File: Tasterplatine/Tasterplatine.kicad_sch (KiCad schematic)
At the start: 3 parts, among them J1 2,5 MSFW 06, SW1 Marquardt 1010.8502

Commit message: pins
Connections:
- net LS: now reaches LA1.1 (-)
- net LS: now also J1.2 (Pin_2); no longer J1.5 (Pin_5)
- net +12V: now reaches J1.4 (Pin_4)
- net +12V: now also SW1.2 (B); no longer LA1.2 (+)
- net ZE5: now reaches SW1.1 (A)
- net ZE5: now also J1.5 (Pin_5); no longer J1.2 (Pin_2)
- net LZ: now reaches J1.3 (Pin_3)
- net LZ: now also LA1.2 (+); no longer SW1.2 (B)
- net FREI: now reaches J1.1 (Pin_1)
- net FREI: no longer SW1.3 (C)
- net TASTE: now reaches J1.6 (Pin_6)
- net TASTE: now also SW1.3 (C)
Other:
- note added: "6V"
- note added: "MINUS"
- moved on the sheet: J1, LA1, SW1
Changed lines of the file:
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@@
 		(comment 1 "4079/030501/E")
 	)
+	(text "MINUS"
+		(exclude_from_sim no)
+		(at 74.93 57.658 90)
+		(effects
+			(font
+				(size 1.27 1.27)
+			)
+		)
+	)
+	(text "6V"
+		(exclude_from_sim no)
+		(at 64.77 58.166 90)
+		(effects
+			(font
+				(size 1.27 1.27)
+			)
+		)
+	)
 	(no_connect
-		(at 74.93 64.77)
-	)
-	(wire
-		(pts
-			(xy 87.63 59.69) (xy 87.63 66.04)
-		)
-		(stroke
-			(width 0)
-			(type default)
-		)
-	)
-	(wire
-		(pts
-			(xy 87.63 76.2) (xy 83.82 76.2)
-		)
-		(stroke
-			(width 0)
-			(type default)
-		)
-	)
-	(wire
-		(pts
-			(xy 92.71 57.15) (xy 92.71 41.91)
-		)
-		(stroke
-			(width 0)
-			(type default)
-		)
-	)
-	(wire
-		(pts
-			(xy 74.93 59.69) (xy 87.63 59.69)
-		)
-		(stroke
-			(width 0)
-			(type default)
-		)
-	)
-	(wire
-		(pts
-			(xy 83.82 62.23) (xy 74.93 62.23)
-		)
-		(stroke
-			(width 0)
-			(type default)
-		)
-	)
-	(wire
-		(pts
-			(xy 95.25 52.07) (xy 95.25 54.61)
-		)
-		(stroke
-			(width 0)
-			(type default)
-		)
-	)
-	(wire
-		(pts
-			(xy 95.25 54.61) (xy 74.93 54.61)
-		)
-		(stroke
-			(width 0)
-			(type default)
-		)
-	)
-	(wire
-		(pts
-			(xy 83.82 76.2) (xy 83.82 62.23)
-		)
-		(stroke
-			(width 0)
-			(type default)
-		)
-	)
-	(wire
-		(pts
-			(xy 74.93 57.15) (xy 92.71 57.15)
-		)
-		(stroke
-			(width 0)
-			(type default)
-		)
-	)
-	(wire
-		(pts
-			(xy 74.93 52.07) (xy 90.17 52.07)
-		)
-		(stroke
-			(width 0)
-			(type default)
+		(at 76.2 73.66)
+	)
+	(wire
+		(pts
+			(xy 81.28 60.96) (xy 74.93 60.96)
+		)
+		(stroke
+			(width 0)
+			(type default)
+		)
+	)
+	(wire
+		(pts
+			(xy 64.77 60.96) (xy 64.77 64.77)
+		)
+		(stroke
+			(width 0)
+			(type default)
+		)
+	)
+	(wire
+		(pts
+			(xy 83.82 55.88) (xy 99.06 55.88)
+		)
+		(stroke
+			(width 0)
+			(type default)
+		)
+	)
+	(wire
+		(pts
+			(xy 81.28 73.66) (xy 81.28 60.96)
+		)
+		(stroke
+			(width 0)
+			(type default)
+		)
+	)
+	(wire
+		(pts
+			(xy 78.74 64.77) (xy 78.74 73.66)
+		)
+		(stroke
+			(width 0)
+			(type default)
+		)
+	)
+	(wire
+		(pts
+			(xy 88.9 53.34) (xy 86.36 53.34)
+		)
+		(stroke
+			(width 0)
+			(type default)
+		)
+	)
+	(wire
+		(pts
+			(xy 86.36 53.34) (xy 86.36 73.66)
+		)
+		(stroke
+			(width 0)
+			(type default)
+		)
+	)
+	(wire
+		(pts
+			(xy 64.77 64.77) (xy 78.74 64.77)
+		)
+		(stroke
+			(width 0)
+			(type default)
+		)
+	)
+	(wire
+		(pts
+			(xy 83.82 73.66) (xy 83.82 55.88)
+		)
+		(stroke
+			(width 0)
+			(type default)
+		)
+	)
+	(wire
+		(pts
+			(xy 88.9 73.66) (xy 88.9 58.42)
+		)
+		(stroke
+			(width 0)
+			(type default)
+		)
+	)
+	(label "FREI"
+		(at 76.2 73.66 90)
+		(effects
+			(font
+				(size 1.27 1.27)
+			)
+			(justify left bottom)
+		)
+	)
+	(label "+12V"
+		(at 83.82 73.66 90)
+		(effects
+			(font
+				(size 1.27 1.27)
+			)
+			(justify left bottom)
+		)
+	)
+	(label "LS"
+		(at 78.74 73.66 90)
+		(effects
+			(font
+				(size 1.27 1.27)
+			)
+			(justify left bottom)
+		)
+	)
+	(label "TASTE"
+		(at 88.9 73.66 90)
+		(effects
+			(font
+				(size 1.27 1.27)
+			)
+			(justify left bottom)
+		)
+	)
+	(label "LZ"
+		(at 81.28 73.66 90)
+		(effects
+			(font
+				(size 1.27 1.27)
+			)
+			(justify left bottom)
+		)
+	)
+	(label "ZE5"
+		(at 86.36 73.66 90)
+		(effects
+			(font
+				(size 1.27 1.27)
+			)
+			(justify left bottom)
 		)
 	)
 	(symbol
 		(lib_id "Device:Lamp")
-		(at 87.63 71.12 0)
+		(at 69.85 60.96 270)
+		(mirror x)
 		(unit 1)
 		(exclude_from_sim no)
@@
 		(fields_autoplaced yes)
 		(property "Reference" "LA1"
-			(at 91.44 69.8499 0)
+			(at 71.1201 57.15 0)
 			(effects
 				(font
@@
 		)
 		(property "Value" "T10 10x27 W2,1x9,5d 6V 2W"
-			(at 91.44 72.3899 0)
+			(at 68.5801 57.15 0)
 			(effects
 				(font
@@
 		)
 		(property "Footprint" "Taster:LampSocket"
-			(at 87.63 68.58 90)
+			(at 72.39 60.96 90)
 			(effects
 				(font
@@
 		)
 		(property "Datasheet" "~"
-			(at 87.63 68.58 90)
+			(at 72.39 60.96 90)
 			(effects
 				(font
@@
 		)
 		(property "Description" "Lamp"
-			(at 87.63 71.12 0)
+			(at 69.85 60.96 0)
 			(effects
 				(font
@@
 	(symbol
 		(lib_id "Switch:SW_Push_SPDT")
-		(at 92.71 46.99 270)
+		(at 93.98 55.88 0)
+		(mirror y)
 		(unit 1)
 		(exclude_from_sim no)
@@
 		(fields_autoplaced yes)
 		(property "Reference" "SW1"
-			(at 97.79 45.7199 90)
+			(at 95.2501 50.8 90)
 			(effects
 				(font
@@
 		)
 		(property "Value" "Marquardt 1010.8502"
-			(at 97.79 48.2599 90)
+			(at 92.7101 50.8 90)
 			(effects
 				(font
@@
 		)
 		(property "Footprint" "Taster:Marquardt1010"
-			(at 92.71 46.99 0)
+			(at 93.98 55.88 0)
 			(effects
 				(font
@@
 		)
 		(property "Datasheet" "~"
-			(at 92.71 46.99 0)
+			(at 93.98 55.88 0)
 			(effects
 				(font
@@
 		)
 		(property "Description" "Momentary Switch, single pole double throw"
-			(at 92.71 46.99 0)
+			(at 93.98 55.88 0)
 			(effects
 				(font
@@
 	(symbol
 		(lib_id "Connector:Conn_01x06_Pin")
-		(at 69.85 57.15 0)
+		(at 81.28 78.74 90)
 		(unit 1)
 		(exclude_from_sim no)
@@
 		(on_board yes)
 		(dnp no)
-		(fields_autoplaced yes)
 		(property "Reference" "J1"
-			(at 70.485 46.99 0)
+			(at 71.12 78.105 0)
 			(effects
 				(font
@@
 		)
 		(property "Value" "2,5 MSFW 06"
-			(at 70.485 49.53 0)
+			(at 73.66 78.105 0)
 			(effects
 				(font
@@
 		)
 		(property "Footprint" "Connector_JST:JST_EH_S6B-EH_1x06_P2.50mm_Horizontal"
-			(at 69.85 57.15 0)
+			(at 81.28 78.74 0)
 			(effects
 				(font
@@
 		)
 		(property "Datasheet" "~"
-			(at 69.85 57.15 0)
+			(at 81.28 78.74 0)
 			(effects
 				(font
@@
 		)
 		(property "Description" "Generic connector, single row, 01x06, script generated"
-			(at 69.85 57.15 0)
-			(effects
-				(font
+			(at 81.28 78.74 0)
+			(effects
+				(font

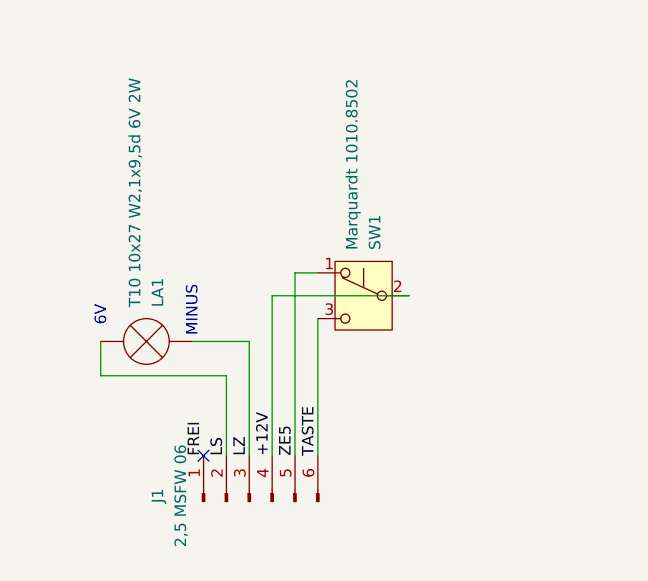
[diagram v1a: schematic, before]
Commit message: taster LED
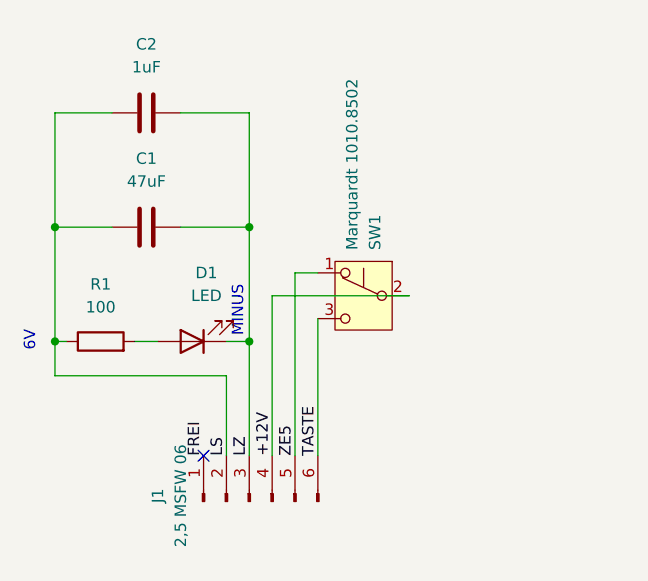
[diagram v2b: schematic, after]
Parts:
- removed LA1: T10 10x27 W2,1x9,5d 6V 2W, Taster:LampSocket, symbol Device:Lamp
- added C1: 47uF, Capacitor_Tantalum_SMD:CP_EIA-3528-12_Kemet-T, symbol Device:C
- added C2: 1uF, Capacitor_SMD:C_1206_3216Metric, symbol Device:C
- added D1: LED, LED_SMD:LED_PLCC_2835_Handsoldering, symbol Device:LED
- added R1: 100, Resistor_SMD:R_1206_3216Metric, symbol Device:R
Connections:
- net LS: now also C1.1, C2.1, R1.1
- net LZ: now also C1.2, C2.2, D1.1 (K)
- new net: D1.2 (A), R1.2
